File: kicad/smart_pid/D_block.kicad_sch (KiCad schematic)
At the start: 15 parts, among them U11 VCA822, U23 DG408DQ-T1-E3

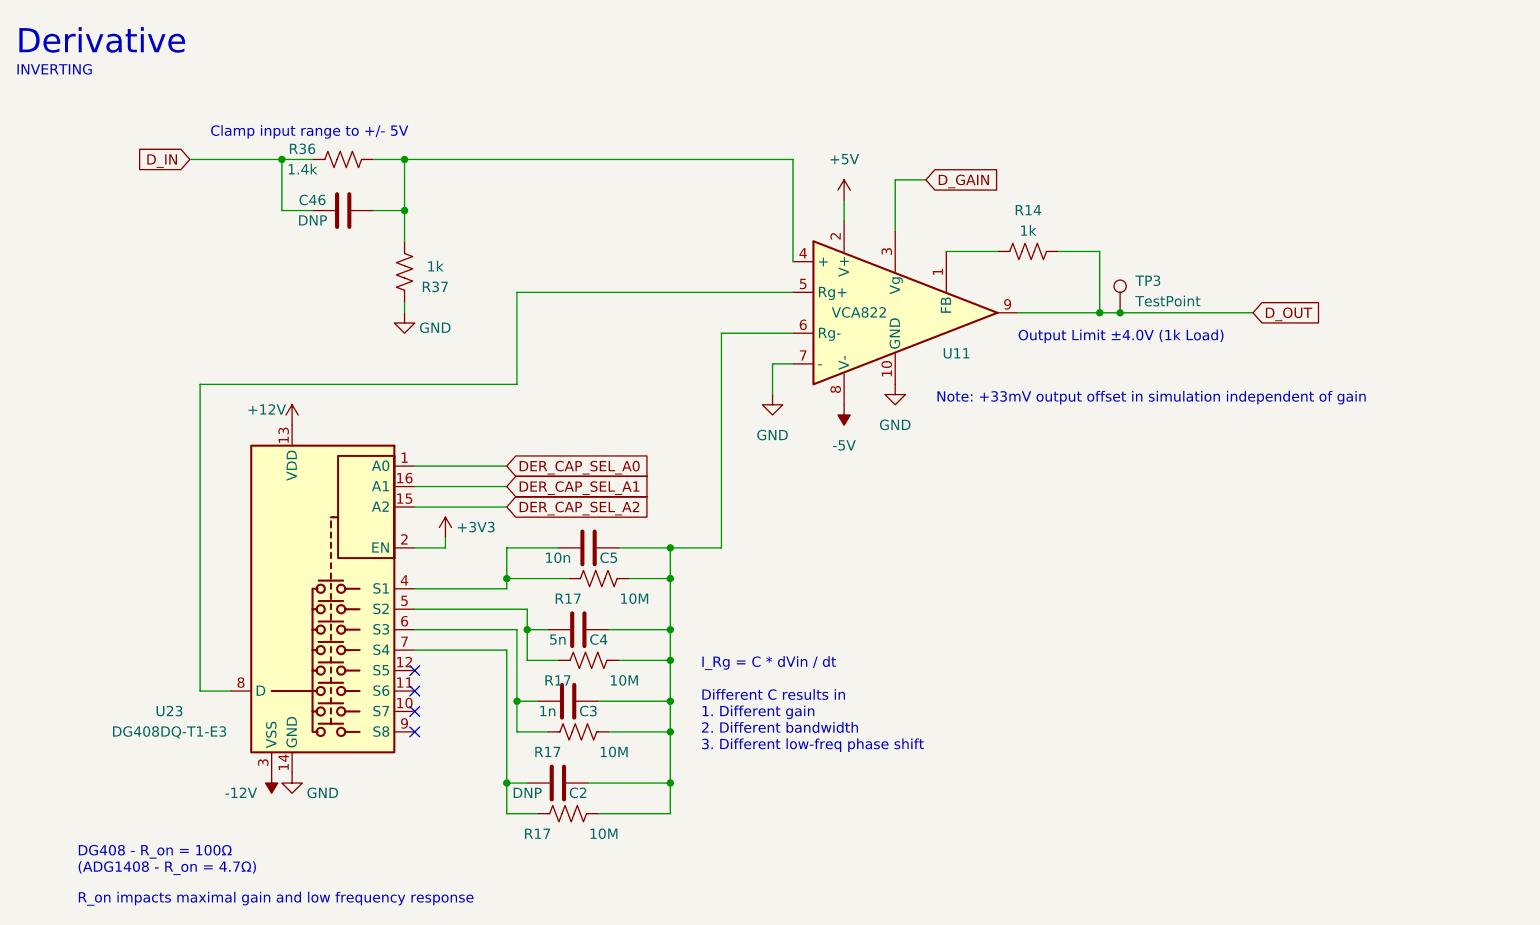
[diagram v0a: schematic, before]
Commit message: Added inverter and modified ext. setpoint disable
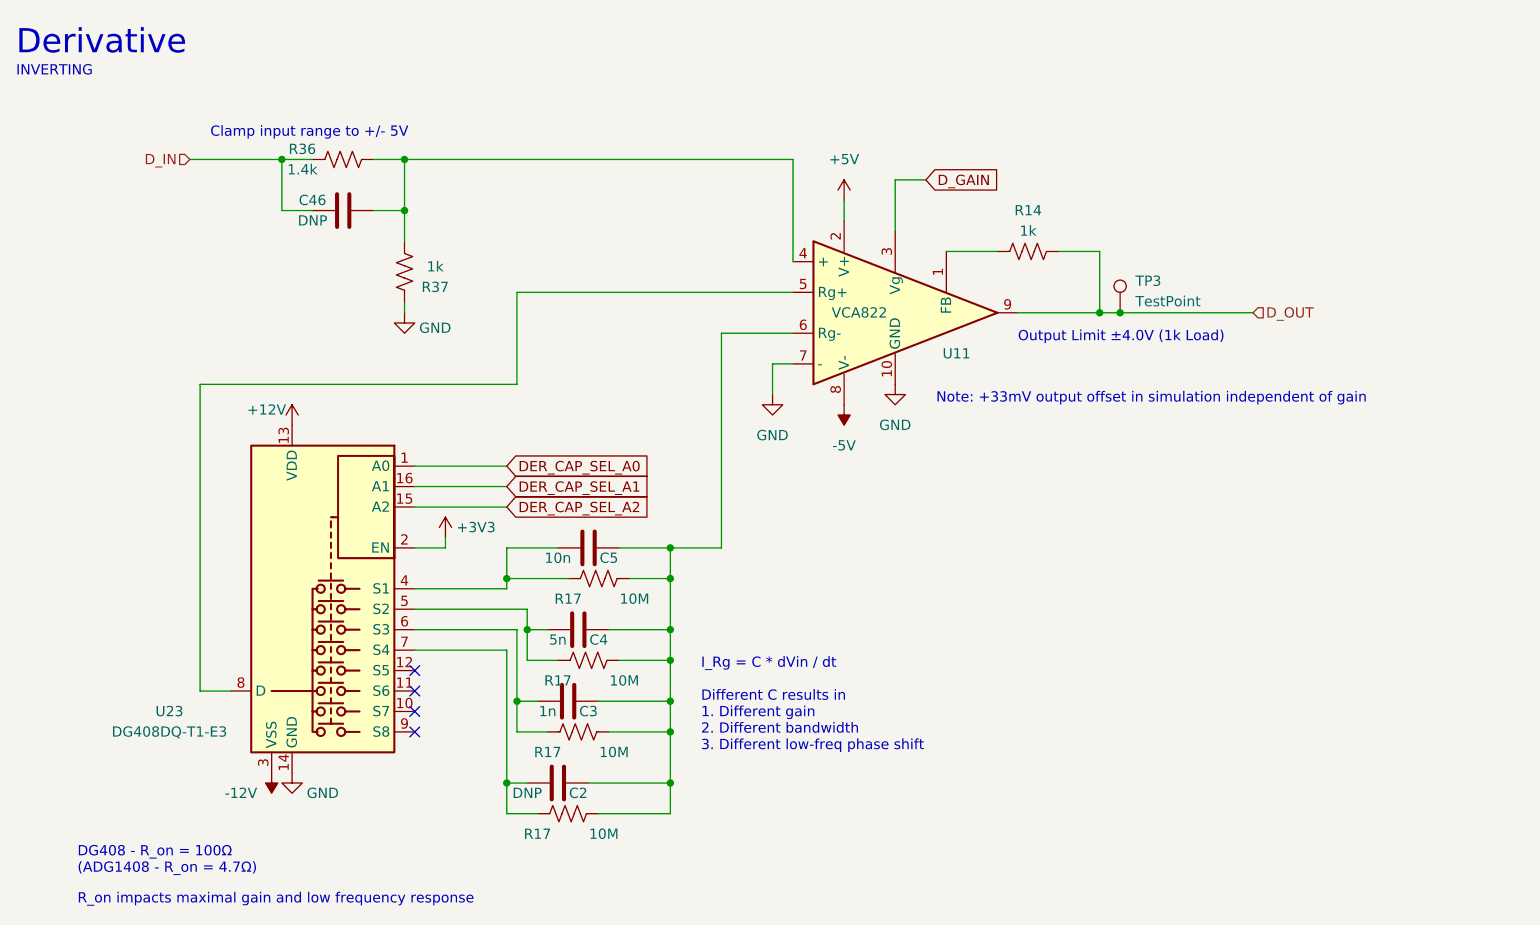
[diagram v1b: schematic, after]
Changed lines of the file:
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@@
-    )
-  )
-  (global_label "D_IN" (shape input) (at 36.83 33.02 180) (fields_autoplaced)
-    (effects (font (size 1.27 1.27)) (justify right))
-    (property "Intersheetrefs" "${INTERSHEET_REFS}" (at 29.6719 33.02 0)
-      (effects (font (size 1.27 1.27)) (justify right) hide)
     )
   )
@@
     )
   )
-  (global_label "D_OUT" (shape input) (at 168.91 52.07 0) (fields_autoplaced)
-    (effects (font (size 1.27 1.27)) (justify left))
-    (property "Intersheetrefs" "${INTERSHEET_REFS}" (at 177.7614 52.07 0)
-      (effects (font (size 1.27 1.27)) (justify left) hide)
-    )
-  )
   (global_label "DER_CAP_SEL_A0" (shape input) (at 76.2 71.12 0) (fields_autoplaced)
     (effects (font (size 1.27 1.27)) (justify left))
@@
     )
   )
+  (hierarchical_label "D_IN" (shape input) (at 36.83 33.02 180) (fields_autoplaced)
+    (effects (font (size 1.27 1.27)) (justify right))
+  )
+  (hierarchical_label "D_OUT" (shape input) (at 168.91 52.07 0) (fields_autoplaced)
+    (effects (font (size 1.27 1.27)) (justify left))
+  )
   (symbol (lib_id "Device:R_US") (at 140.97 44.45 90) (unit 1)
